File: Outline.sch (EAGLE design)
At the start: 51 parts, among them CN1 0675031020, IC1 ATXMEGA32A4U-AU, IC2 ST1480ACDR, J1 RJHSE5080, J2 J2, U1 NCP1117DTAG @ 3.3v, U2 NCP1117DTAG @ 12v

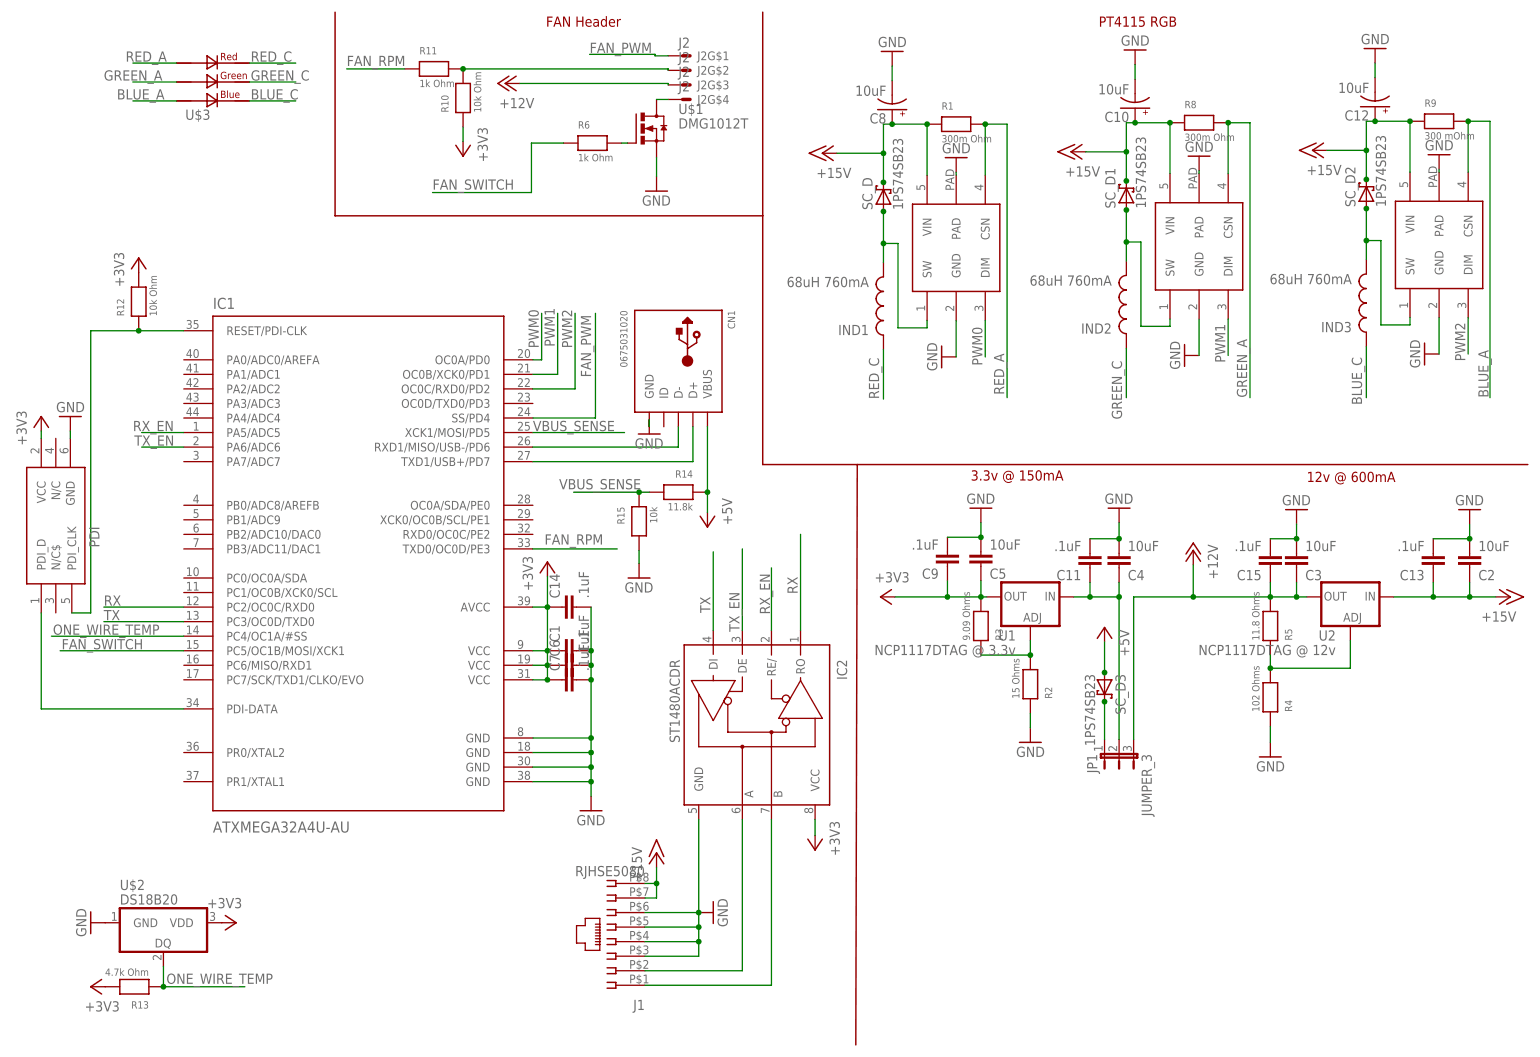
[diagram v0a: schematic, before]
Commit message: 4.3
Changed LDO resistor values to stop overheating. Added 68pf cap between
reset and ground to make AVR Dragon talk with device.
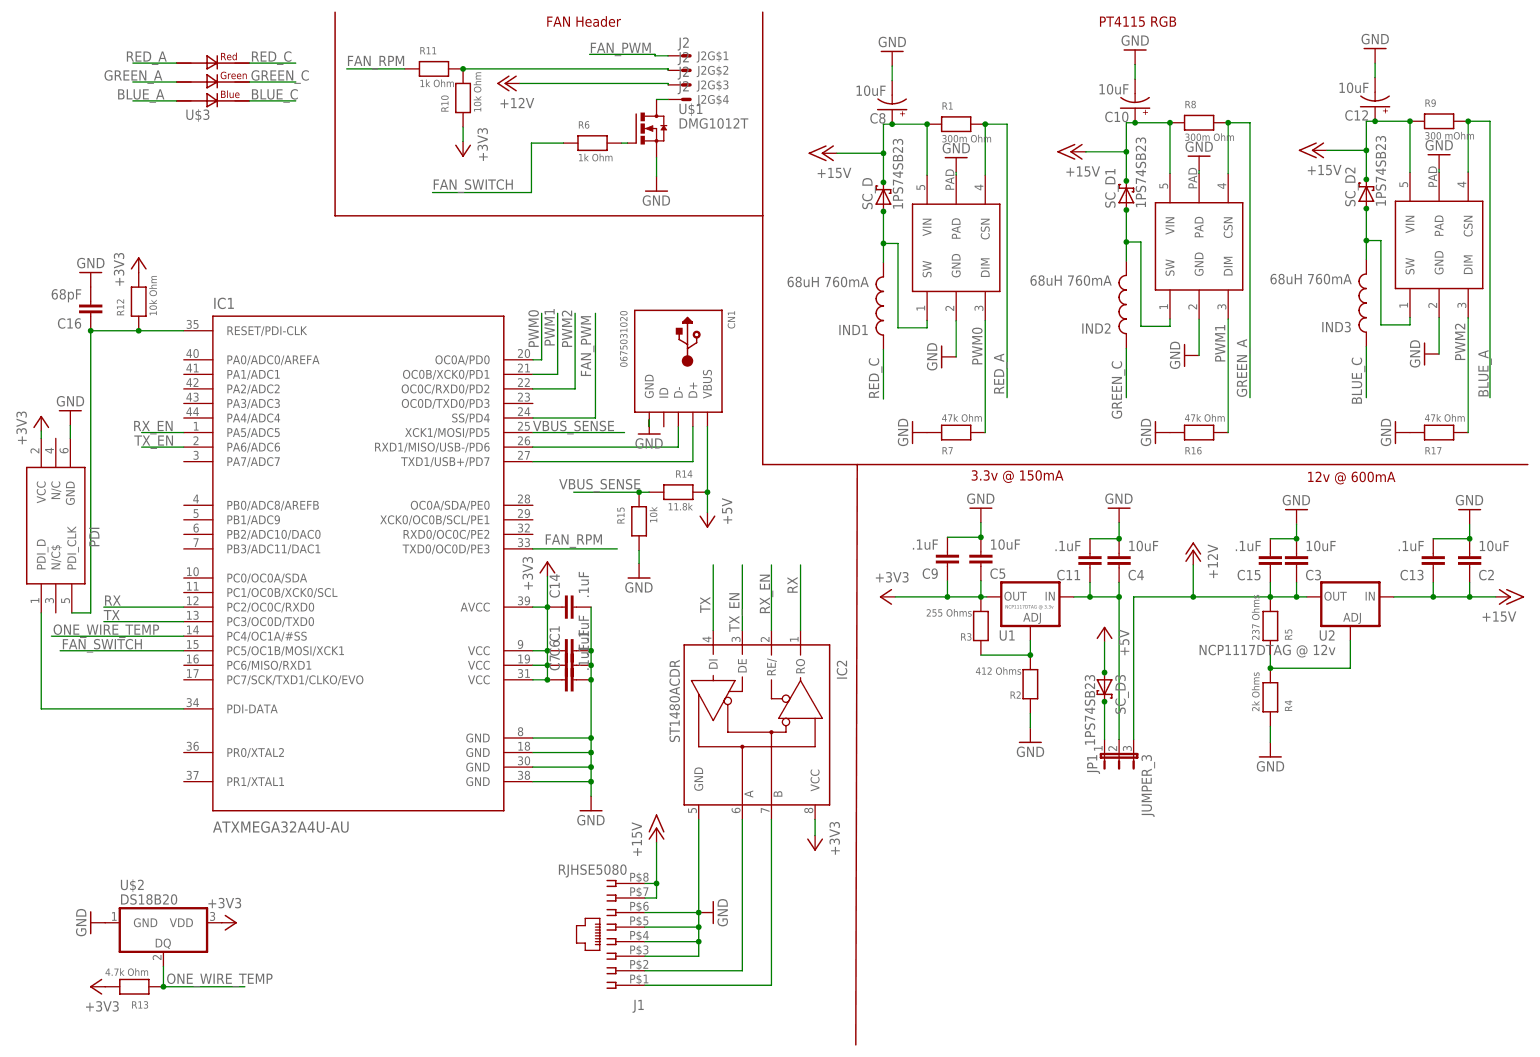
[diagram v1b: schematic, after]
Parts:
- added C16: 68pF, SparkFun:CAP0603-CAP
- added R16, R17, R7: 47k Ohm, nonolith:RESISTOR0603
- R2: value 15 Ohms -> 412 Ohms
- R3: value 9.09 Ohms -> 255 Ohms
- R4: value 102 Ohms -> 2k Ohms
- R5: value 11.8 Ohms -> 237 Ohms
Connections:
- net GND: now also C16.2, R16.1, R17.1, R7.1
- net N$22: now also C16.1
- net PWM0: now also R7.2
- net PWM1: now also R16.2
- net PWM2: now also R17.2
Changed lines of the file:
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@@
 <parts>
 <part name="IC1" library="nonolith" deviceset="ATXMEGAXXA4U" device="-AU" value="ATXMEGA32A4U-AU"/>
-<part name="R2" library="nonolith" deviceset="RESISTOR" device="0603" value="15 Ohms"/>
-<part name="R3" library="nonolith" deviceset="RESISTOR" device="0603" value="9.09 Ohms"/>
-<part name="R4" library="nonolith" deviceset="RESISTOR" device="0603" value="102 Ohms"/>
-<part name="R5" library="nonolith" deviceset="RESISTOR" device="0603" value="11.8 Ohms"/>
+<part name="R2" library="nonolith" deviceset="RESISTOR" device="0603" value="412 Ohms"/>
+<part name="R3" library="nonolith" deviceset="RESISTOR" device="0603" value="255 Ohms"/>
+<part name="R4" library="nonolith" deviceset="RESISTOR" device="0603" value="2k Ohms"/>
+<part name="R5" library="nonolith" deviceset="RESISTOR" device="0603" value="237 Ohms"/>
 <part name="C1" library="SparkFun" deviceset="CAP" device="0603-CAP" value=".1uF"/>
 <part name="C2" library="SparkFun" deviceset="CAP" device="1210" value="10uF"/>
@@
 <part name="SC_D3" library="TechIsCool" deviceset="SCHOTTKY_2" device="" value="1PS74SB23"/>
 <part name="U$3" library="TechIsCool" deviceset="10W_RGB_LED" device=""/>
+<part name="C16" library="SparkFun" deviceset="CAP" device="0603-CAP" value="68pF"/>
+<part name="GND6" library="supply1" deviceset="GND" device=""/>
+<part name="R7" library="nonolith" deviceset="RESISTOR" device="0603" value="47k Ohm"/>
+<part name="R16" library="nonolith" deviceset="RESISTOR" device="0603" value="47k Ohm"/>
+<part name="R17" library="nonolith" deviceset="RESISTOR" device="0603" value="47k Ohm"/>
+<part name="GND7" library="supply1" deviceset="GND" device=""/>
+<part name="GND25" library="supply1" deviceset="GND" device=""/>
+<part name="GND26" library="supply1" deviceset="GND" device=""/>
 </parts>
 <sheets>
@@
 <instances>
 <instance part="IC1" gate="G$1" x="60.198" y="84.074"/>
-<instance part="R2" gate="G$1" x="177.546" y="62.992" rot="MR90"/>
-<instance part="R3" gate="G$1" x="168.91" y="73.152" rot="MR90"/>
+<instance part="R2" gate="G$1" x="177.546" y="62.992" smashed="yes" rot="MR90">
+<attribute name="NAME" x="176.022" y="60.452" size="1.27" layer="95" font="vector" rot="MR0"/>
+<attribute name="VALUE" x="176.022" y="64.643" size="1.27" layer="96" font="vector" rot="MR0"/>
+</instance>
+<instance part="R3" gate="G$1" x="168.91" y="73.152" smashed="yes" rot="MR90">
+<attribute name="NAME" x="167.386" y="70.612" size="1.27" layer="95" font="vector" rot="MR0"/>
+<attribute name="VALUE" x="167.386" y="74.803" size="1.27" layer="96" font="vector" rot="MR0"/>
+</instance>
 <instance part="R4" gate="G$1" x="219.456" y="60.706" rot="MR90"/>
 <instance part="R5" gate="G$1" x="219.456" y="73.152" rot="MR90"/>
@@
 <instance part="C4" gate="G$1" x="193.04" y="85.852" rot="MR180"/>
 <instance part="C5" gate="G$1" x="168.91" y="86.106" rot="MR180"/>
-<instance part="U1" gate="G$1" x="177.546" y="78.232" rot="MR0"/>
+<instance part="U1" gate="G$1" x="177.546" y="78.232" smashed="yes" rot="MR0">
+<attribute name="NAME" x="175.006" y="70.612" size="1.778" layer="95" rot="MR0"/>
+<attribute name="VALUE" x="181.61" y="76.2" size="0.6096" layer="96" rot="MR0"/>
+</instance>
 <instance part="U2" gate="G$1" x="233.426" y="78.232" rot="MR0"/>
 <instance part="+3V1" gate="G$1" x="151.384" y="78.232" rot="MR270"/>
@@
 <instance part="P+6" gate="1" x="226.822" y="156.21" rot="R90"/>
 <instance part="R9" gate="G$1" x="248.92" y="161.29"/>
-<instance part="J1" gate="G$1" x="105.156" y="18.034" rot="R180"/>
+<instance part="J1" gate="G$1" x="105.156" y="18.034" smashed="yes" rot="R180">
+<attribute name="NAME" x="110.236" y="7.874" size="1.778" layer="95" rot="R180"/>
+<attribute name="VALUE" x="107.188" y="31.496" size="1.778" layer="96" rot="R180"/>
+</instance>
 <instance part="IC2" gate="G$1" x="127.254" y="59.69" rot="R270"/>
-<instance part="P+7" gate="1" x="112.268" y="33.528"/>
+<instance part="P+7" gate="1" x="112.268" y="37.846"/>
 <instance part="+3V5" gate="G$1" x="139.954" y="34.036" rot="R180"/>
 <instance part="CN1" gate="G$1" x="116.078" y="119.38" rot="R270"/>
@@
 <instance part="P+9" gate="1" x="121.158" y="90.424" rot="R180"/>
 <instance part="PDI" gate="G$1" x="14.986" y="86.868" rot="R90"/>
-<instance part="GND22" gate="1" x="9.906" y="109.728" rot="R180"/>
+<instance part="GND22" gate="1" x="9.906" y="110.744" rot="R180"/>
 <instance part="+3V6" gate="G$1" x="4.826" y="109.728"/>
 <instance part="GND23" gate="1" x="112.268" y="149.098"/>
@@
 <instance part="SC_D3" gate="G$1" x="190.5" y="62.484" rot="R270"/>
 <instance part="U$3" gate="1" x="35.56" y="168.148"/>
+<instance part="C16" gate="G$1" x="13.462" y="129.794" rot="R180"/>
+<instance part="GND6" gate="1" x="13.462" y="134.874" rot="R180"/>
+<instance part="R7" gate="G$1" x="164.592" y="106.934" rot="MR180"/>
+<instance part="R16" gate="G$1" x="207.01" y="106.934" rot="MR180"/>
+<instance part="R17" gate="G$1" x="248.92" y="106.934" rot="MR180"/>
+<instance part="GND7" gate="1" x="241.3" y="106.934" rot="R270"/>
+<instance part="GND25" gate="1" x="199.39" y="106.934" rot="R270"/>
+<instance part="GND26" gate="1" x="156.972" y="106.934" rot="R270"/>
 </instances>
 <busses>
@@
 <pinref part="P+7" gate="1" pin="+15V"/>
 <wire x1="110.236" y1="28.194" x2="112.268" y2="28.194" width="0.1524" layer="91"/>
-<wire x1="112.268" y1="28.194" x2="112.268" y2="30.988" width="0.1524" layer="91"/>
+<wire x1="112.268" y1="28.194" x2="112.268" y2="35.306" width="0.1524" layer="91"/>
 <pinref part="J1" gate="G$1" pin="7"/>
 <wire x1="110.236" y1="25.654" x2="112.268" y2="25.654" width="0.1524" layer="91"/>
@@
 <pinref part="PDI" gate="G$1" pin="GND"/>
 <pinref part="GND22" gate="1" pin="GND"/>
-<wire x1="9.906" y1="105.918" x2="9.906" y2="107.188" width="0.1524" layer="91"/>
+<wire x1="9.906" y1="105.918" x2="9.906" y2="108.204" width="0.1524" layer="91"/>
 </segment>
 <segment>
@@
 <wire x1="112.268" y1="151.638" x2="112.268" y2="154.94" width="0.1524" layer="91"/>
 </segment>
+<segment>
+<pinref part="C16" gate="G$1" pin="2"/>
+<pinref part="GND6" gate="1" pin="GND"/>
+</segment>
+<segment>
+<pinref part="R17" gate="G$1" pin="1"/>
+<pinref part="GND7" gate="1" pin="GND"/>
+</segment>
+<segment>
+<pinref part="R16" gate="G$1" pin="1"/>
+<pinref part="GND25" gate="1" pin="GND"/>
+</segment>
+<segment>
+<pinref part="R7" gate="G$1" pin="1"/>
+<pinref part="GND26" gate="1" pin="GND"/>
+</segment>
 </net>
 <net name="+12V" class="0">
@@
 <net name="PWM0" class="0">
 <segment>
-<wire x1="169.672" y1="126.492" x2="169.672" y2="120.142" width="0.1524" layer="91"/>
+<wire x1="169.672" y1="126.492" x2="169.672" y2="106.934" width="0.1524" layer="91"/>
 <label x="169.164" y="118.618" size="1.778" layer="95" rot="R90"/>
 <pinref part="DRV0" gate="G$1" pin="DIM"/>
+<pinref part="R7" gate="G$1" pin="2"/>
 </segment>
 <segment>
@@
 <segment>
 <pinref part="DRV1" gate="G$1" pin="DIM"/>
-<wire x1="212.09" y1="126.746" x2="212.09" y2="120.396" width="0.1524" layer="91"/>
+<wire x1="212.09" y1="126.746" x2="212.09" y2="106.934" width="0.1524" layer="91"/>
 <label x="211.582" y="119.126" size="1.778" layer="95" rot="R90"/>
+<pinref part="R16" gate="G$1" pin="2"/>
 </segment>
 <segment>
@@
 <segment>
 <pinref part="DRV2" gate="G$1" pin="DIM"/>
-<wire x1="254" y1="127" x2="254" y2="120.65" width="0.1524" layer="91"/>
+<wire x1="254" y1="127" x2="254" y2="106.934" width="0.1524" layer="91"/>
 <label x="253.492" y="119.38" size="1.778" layer="95" rot="R90"/>
+<pinref part="R17" gate="G$1" pin="2"/>
 </segment>
 <segment>
@@
 <wire x1="21.844" y1="124.714" x2="29.718" y2="124.714" width="0.1524" layer="91"/>
 <junction x="21.844" y="124.714"/>
+<pinref part="C16" gate="G$1" pin="1"/>
+<junction x="13.462" y="124.714"/>
 </segment>
 </net>
@@
 <segment>
 <pinref part="IC2" gate="G$1" pin="RO"/>
-<wire x1="137.414" y1="89.154" x2="137.414" y2="72.39" width="0.1524" layer="91"/>
+<wire x1="137.414" y1="83.82" x2="137.414" y2="72.39" width="0.1524" layer="91"/>
 <label x="136.906" y="78.74" size="1.778" layer="95" rot="R90"/>
 </segment>
@@
 <segment>
 <pinref part="IC2" gate="G$1" pin="RE/"/>
-<wire x1="132.334" y1="72.39" x2="132.334" y2="83.312" width="0.1524" layer="91"/>
+<wire x1="132.334" y1="72.39" x2="132.334" y2="83.82" width="0.1524" layer="91"/>
 <label x="132.08" y="75.184" size="1.778" layer="95" rot="R90"/>
 </segment>
@@
 <segment>
 <pinref part="IC2" gate="G$1" pin="DE"/>
-<wire x1="127.254" y1="72.39" x2="127.254" y2="86.614" width="0.1524" layer="91"/>
+<wire x1="127.254" y1="72.39" x2="127.254" y2="83.82" width="0.1524" layer="91"/>
 <label x="126.746" y="72.136" size="1.778" layer="95" rot="R90"/>
 </segment>
@@
 <segment>
 <pinref part="IC2" gate="G$1" pin="DI"/>
-<wire x1="122.174" y1="72.39" x2="122.174" y2="86.106" width="0.1524" layer="91"/>
+<wire x1="122.174" y1="72.39" x2="122.174" y2="83.82" width="0.1524" layer="91"/>
 <label x="121.666" y="75.438" size="1.778" layer="95" rot="R90"/>
 </segment>
